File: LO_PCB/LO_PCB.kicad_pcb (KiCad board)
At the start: 4 copper layers, 50 x 44 mm, 96 parts, among them J1 PWR, J2 Conn_01x06, Q1 AO3401A, U1 TPS7A9101DSKT, U2 LMX2582RHAR, X1 TB612-100.0M

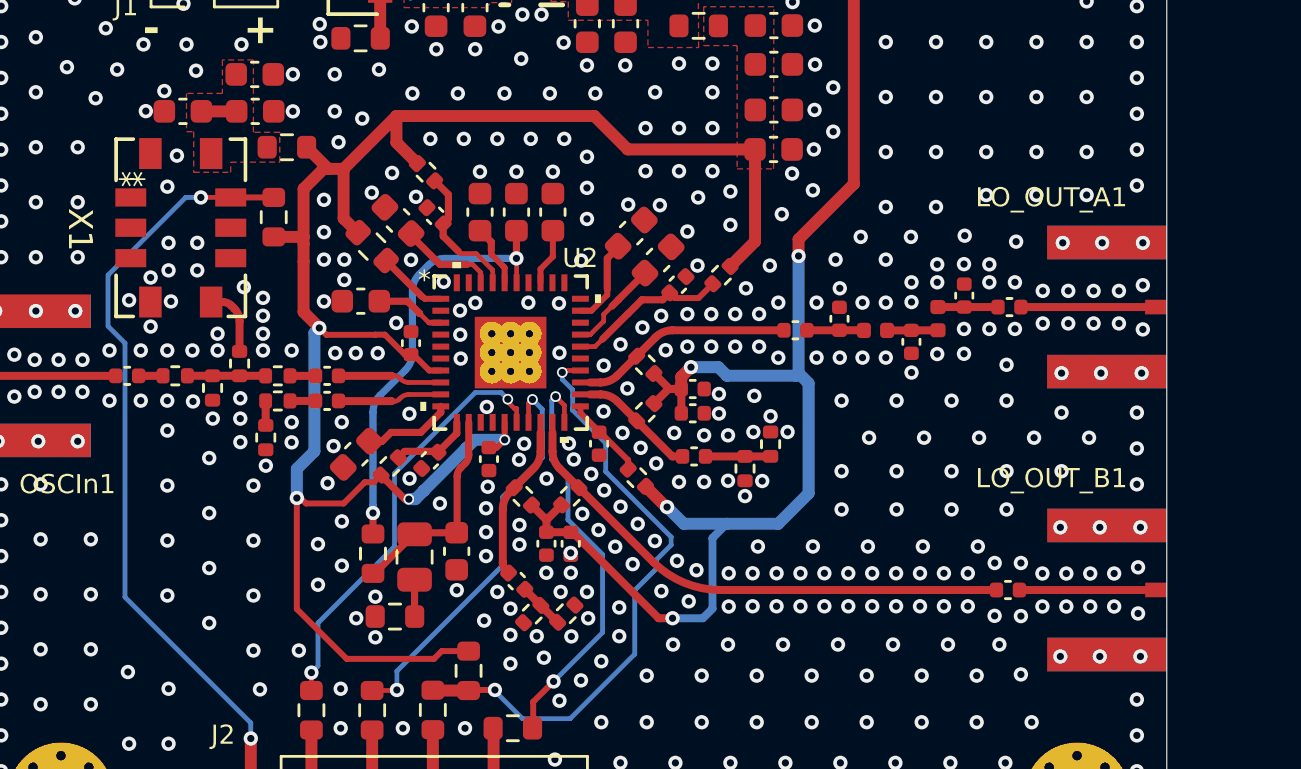
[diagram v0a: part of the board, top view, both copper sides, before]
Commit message: pulled away silkscreen over rf traces and other smaller fixes
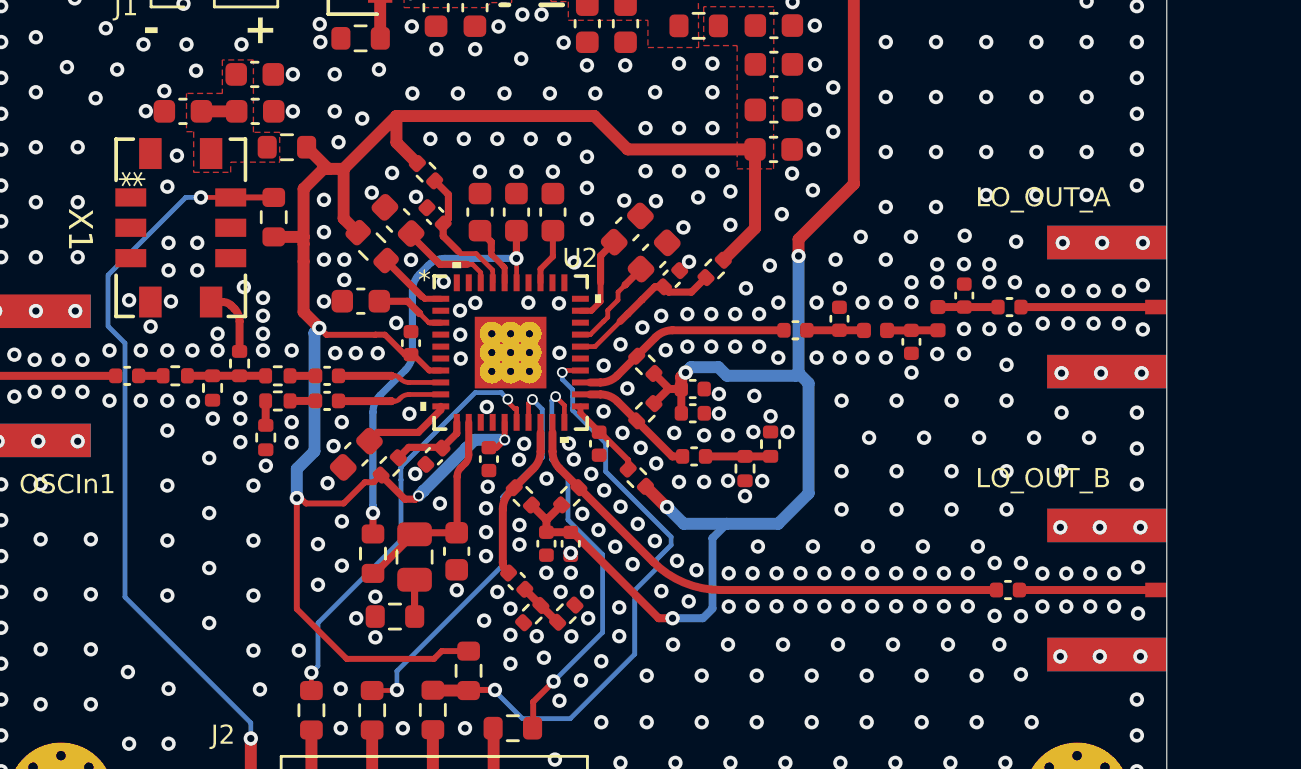
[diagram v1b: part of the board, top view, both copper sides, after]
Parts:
- moved R8 0.39 mm to (166.1, 95.0)
- moved C28 0.36 mm to (164.3, 95.4)
- moved C31 0.24 mm to (154.3, 102.8)
- moved C39 0.24 mm to (162.4, 93.3)
- moved C41 0.24 mm to (163.6, 94.4)
- renumbered LO_OUT_A1 to LO_OUT_A, LO_OUT_B1 to LO_OUT_B
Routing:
- net GND: vias 595 -> 594

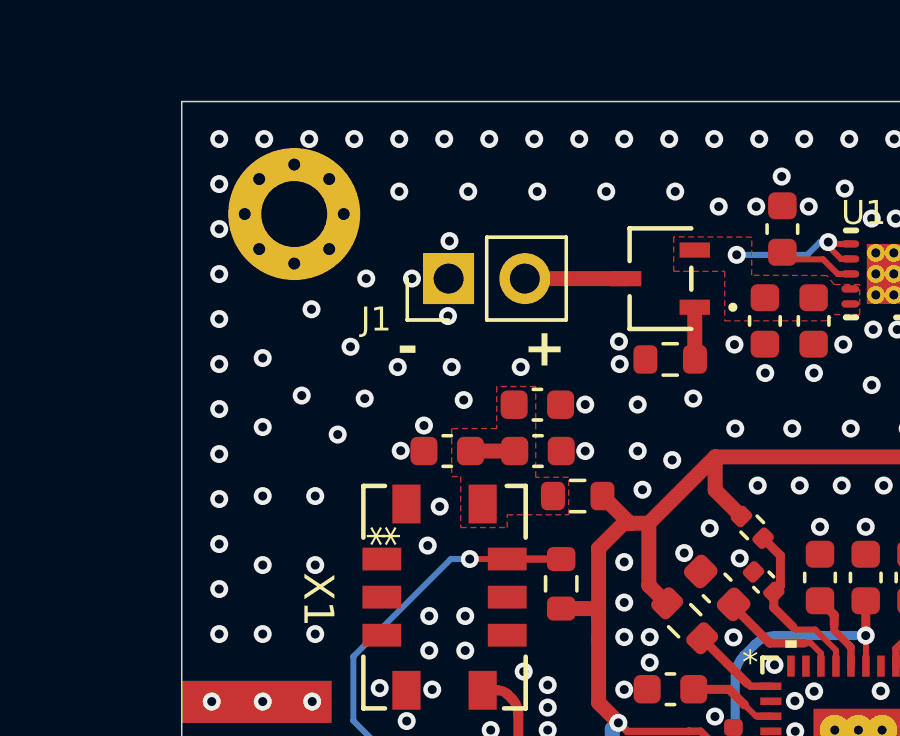
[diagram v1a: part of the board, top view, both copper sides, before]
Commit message: added silkscreen graphic
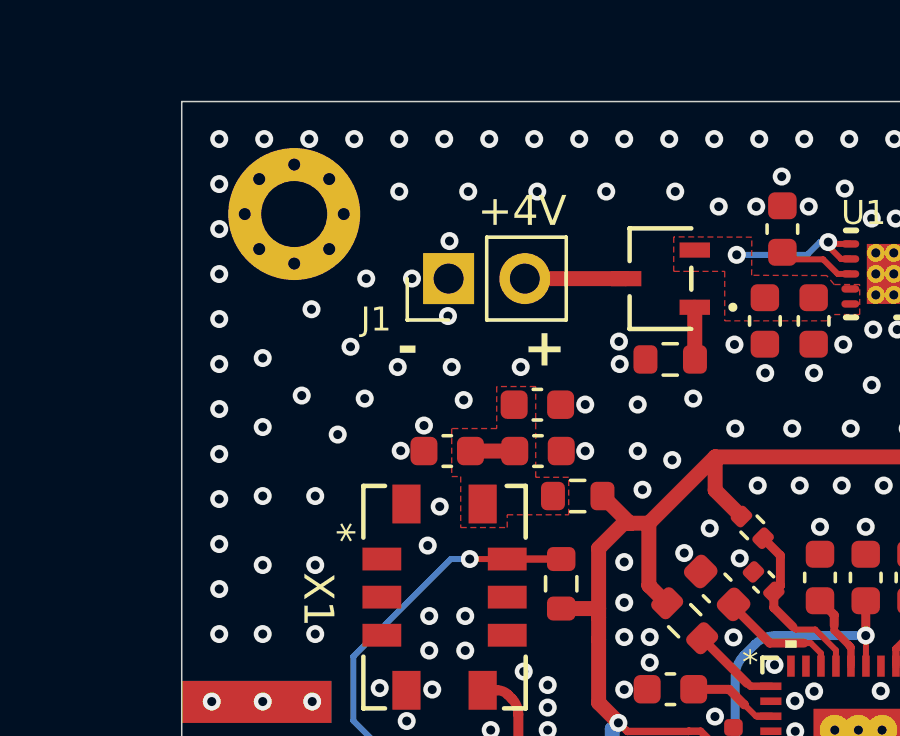
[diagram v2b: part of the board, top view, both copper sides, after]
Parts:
- added G***: LOGO, Snapeda:eye, B.Cu at (159.9, 97.4)
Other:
- board text added: "+4V"

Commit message: maybe final??
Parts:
- renumbered OSCIn1 to EXT_OSC_IN
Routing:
- net GND: vias 594 -> 596
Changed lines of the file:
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@@
 		(descr "PCB End Launch, https://www.we-online.com/en/components/products/datasheet/60312202114513?ki")
 		(tags "SMT")
-		(property "Reference" "OSCIn1"
+		(property "Reference" "EXT_OSC_IN"
 			(at 4.5378 -2.007799 0)
 			(unlocked yes)
@@
 	)
 	(via
+		(at 150.622 81.6356)
+		(size 0.6)
+		(drill 0.3)
+		(layers "F.Cu" "B.Cu")
+		(free yes)
+		(tenting
+			(front yes)
+			(back yes)
+		)
+		(capping no)
+		(covering
+			(front no)
+			(back no)
+		)
+		(plugging
+			(front yes)
+			(back yes)
+		)
+		(filling no)
+		(net "GND")
+	)
+	(via
 		(at 143.25 117.15)
 		(size 0.6)
@@
 		(size 0.6)
 		(drill 0.3)
+		(layers "F.Cu" "B.Cu")
+		(free yes)
+		(tenting
+			(front yes)
+			(back yes)
+		)
+		(capping no)
+		(covering
+			(front no)
+			(back no)
+		)
+		(plugging
+			(front yes)
+			(back yes)
+		)
+		(filling no)
+		(net "GND")
+	)
+	(via
+		(at 150.622 83.693)
+		(size 0.6)
+		(drill 0.3)

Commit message: fixed errors and small bugs
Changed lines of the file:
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@@
 	)
 	(via
-		(at 165.02 94.69)
+		(at 165.1 94.6404)
 		(size 0.6)
 		(drill 0.3)
@@
 	)
 	(segment
-		(start 162.35 95.657092)
-		(end 163.011992 94.9951)
-		(width 0.3)
-		(layer "F.Cu")
-		(net "Net-(U2-VBIASVCO2)")
-	)
-	(segment
-		(start 162.05 96.292092)
-		(end 161.62 96.722092)
+		(start 161.62 97.01)
+		(end 161.455 97.175)
 		(width 0.2)
 		(layer "F.Cu")
@@
 	)
 	(segment
-		(start 160.886201 97.738799)
-		(end 160.476201 97.738799)
+		(start 161.45 97.175)
+		(end 160.886201 97.738799)
 		(width 0.2)
 		(layer "F.Cu")
@@
 	)
 	(segment
-		(start 161.62 97.01)
-		(end 161.455 97.175)
-		(width 0.2)
+		(start 162.35 95.66)
+		(end 162.35 95.657092)
+		(width 0.3)
 		(layer "F.Cu")
 		(net "Net-(U2-VBIASVCO2)")
 	)
 	(segment
-		(start 163.168446 95.1651)
-		(end 163.176992 95.1651)
-		(width 0.25)
+		(start 162.05 96.292092)
+		(end 161.62 96.722092)
+		(width 0.2)
 		(layer "F.Cu")
 		(net "Net-(U2-VBIASVCO2)")
 	)
 	(segment
-		(start 162.35 95.65)
-		(end 162.35 95.66)
+		(start 160.886201 97.738799)
+		(end 160.476201 97.738799)
 		(width 0.2)
 		(layer "F.Cu")
@@
 	)
 	(segment
-		(start 163.153982 95.1401)
-		(end 163.130621 95.1401)
+		(start 163.168446 95.1651)
+		(end 163.176992 95.1651)
 		(width 0.25)
 		(layer "F.Cu")
@@
 	)
 	(segment
-		(start 161.62 96.722092)
-		(end 161.62 97.01)
-		(width 0.2)
+		(start 163.153982 95.1401)
+		(end 163.130621 95.1401)
+		(width 0.25)
 		(layer "F.Cu")
 		(net "Net-(U2-VBIASVCO2)")
 	)
 	(segment
-		(start 162.35 95.66)
-		(end 162.35 95.657092)
+		(start 162.35 95.657092)
+		(end 163.011992 94.9951)
 		(width 0.3)
 		(layer "F.Cu")
@@
 	)
 	(segment
-		(start 162.05 95.96)
-		(end 162.05 96.292092)
+		(start 161.62 96.722092)
+		(end 161.62 97.01)
 		(width 0.2)
 		(layer "F.Cu")
@@
 	)
 	(segment
-		(start 161.45 97.175)
-		(end 160.886201 97.738799)
+		(start 162.05 95.96)
+		(end 162.05 96.292092)
 		(width 0.2)
 		(layer "F.Cu")
@@
 	)
 	(segment
-		(start 162.138117 97.188117)
-		(end 162.461335 96.8649)
-		(width 0.3)
-		(layer "F.Cu")
-		(net "Net-(U2-VCCVCO2)")
-	)
-	(segment
-		(start 162.4649 96.8649)
-		(end 163.05 96.2798)
-		(width 0.3)
-		(layer "F.Cu")
-		(net "Net-(U2-VCCVCO2)")
-	)
-	(segment
 		(start 161.087435 98.2388)
 		(end 160.476201 98.2388)
@@
 	)
 	(segment
-		(start 162.461335 96.8649)
-		(end 162.4649 96.8649)
+		(start 162.138117 97.188117)
+		(end 162.141883 97.188117)
 		(width 0.3)
 		(layer "F.Cu")
@@
 	)
 	(segment
-		(start 163.05 96.2798)
-		(end 163.0502 96.2798)
-		(width 0.3)
-		(layer "F.Cu")
-		(net "Net-(U2-VCCVCO2)")
-	)
-	(segment
-		(start 165.121386 95.958614)
-		(end 165.729375 95.350625)
+		(start 162.141883 97.188117)
+		(end 163.590589 95.739411)
 		(width 0.3)
 		(layer "F.Cu")
@@
 	)
 	(segment
-		(start 163.0502 96.2798)
-		(end 163.590589 95.739411)
+		(start 165.121386 95.958614)
+		(end 165.729375 95.350625)
 		(width 0.3)
 		(layer "F.Cu")

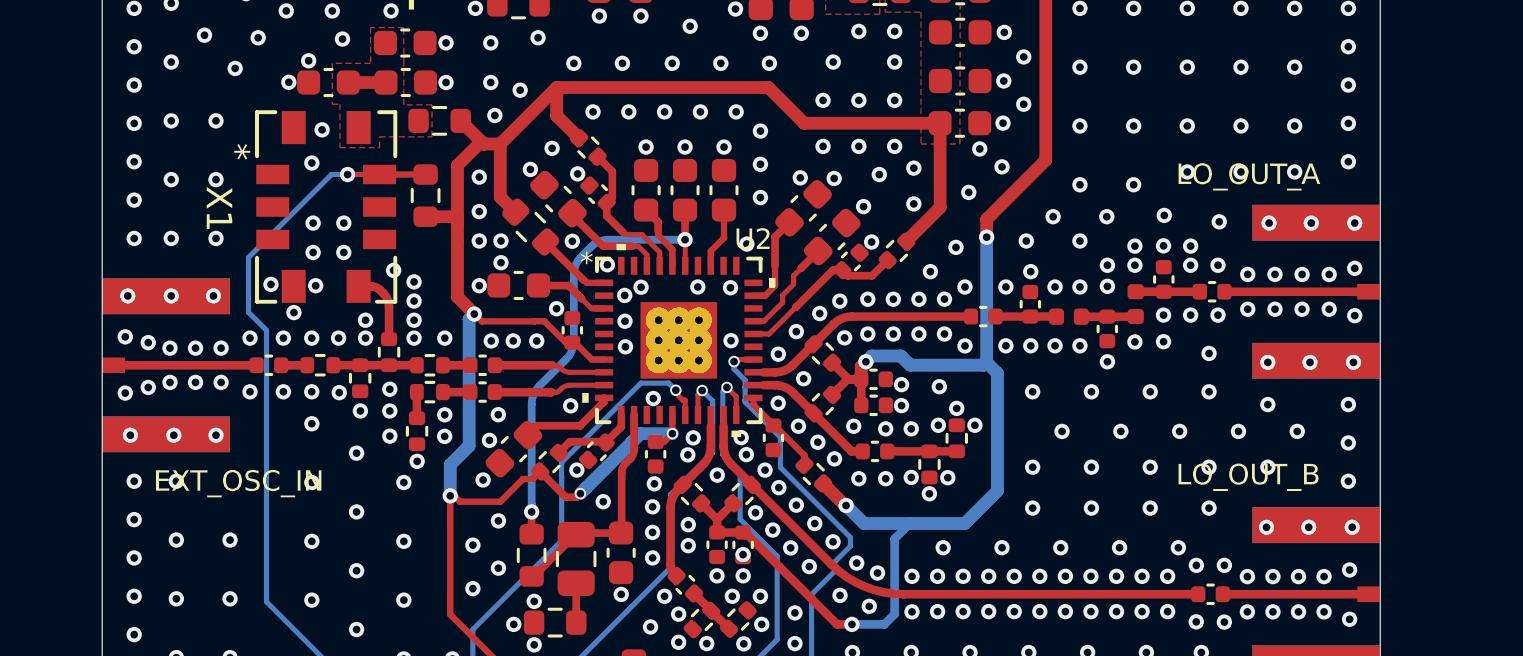
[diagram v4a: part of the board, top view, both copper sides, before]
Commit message: added a tuning parallel cap for ref xo output to better match expected drive. todo: tune resistor values to better suit the TCXO
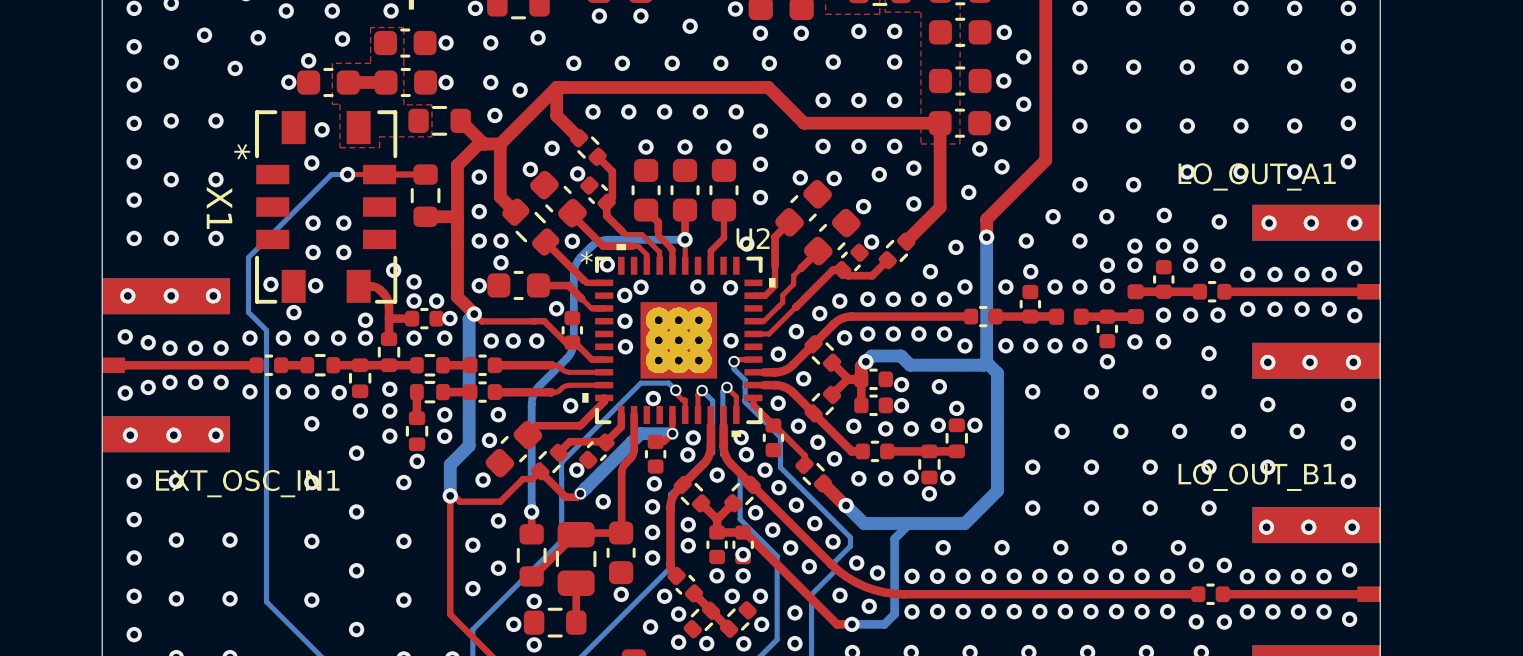
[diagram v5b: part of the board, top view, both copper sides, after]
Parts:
- added C46: 0.1uF, Capacitor_SMD:C_0402_1005Metric, F.Cu at (147.6, 97.6)
- renumbered C46 to C47, C47 to C48, C48 to C49, EXT_OSC_IN to EXT_OSC_IN1, LO_OUT_A to LO_OUT_A1, LO_OUT_B to LO_OUT_B1
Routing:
- net Net-(X1-OUTPUT): track 2.90 -> 3.81 mm
- net GND: vias 596 -> 597

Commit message: final final LO PCB?
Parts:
- added C50: 0.1uF, Capacitor_SMD:C_0402_1005Metric, F.Cu at (146.2, 96.7)
- C46: value 0.1uF -> 15pF
- EXT_REF_IN1: renamed from EXT_OSC_IN1; value OSCinP -> EXT_REF_IN
- R29: value 68 -> 56
- R30: value 68 -> 36
- moved C43 1.43 mm to (143.8, 87.0)
- moved C44 1.43 mm to (146.9, 87.0)
- moved R21 1.43 mm to (148.2, 88.5)
- moved C45 1.42 mm to (146.9, 85.4)
- moved R22 1.42 mm to (147.7, 91.4)
- moved X1 1.42 mm to (143.8, 91.8)
- moved C46 1.41 mm to (147.6, 96.2)
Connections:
- R23 pad 1: Net-(X1-OUTPUT) -> Net-(C50-Pad1)
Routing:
- net VCC: track 78.3 -> 81.0 mm
- net /INT_OSC_ENABLE: track 32.3 -> 33.7 mm
- net Net-(C50-Pad1): track 0.00 -> 1.29 mm
- net Net-(X1-OUTPUT): track 3.81 -> 3.17 mm
- net GND: vias 597 -> 600
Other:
- board text added: "EXT_REF_IN"
- board text added: "LO_OUT_A"
- board text added: "LO_OUT_B"

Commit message: generated gerbers
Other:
- board text added: "LO_BOARD V1.0"

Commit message: updated the LO schematic to better match the external reference usecase
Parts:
- C47, C48, C49: value 0.1uF -> 1nF
- R23: value 47 -> 62
- R27: value 18 -> 0
- R29: value 56 -> 68
- R30: value 36 -> 49.9
